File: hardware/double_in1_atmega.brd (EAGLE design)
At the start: 75 x 35 mm, 37 parts, among them IC1 MEGA8-AI, J1 AVR-ISP-6PINAVR-ISP-6PIN-SMAL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

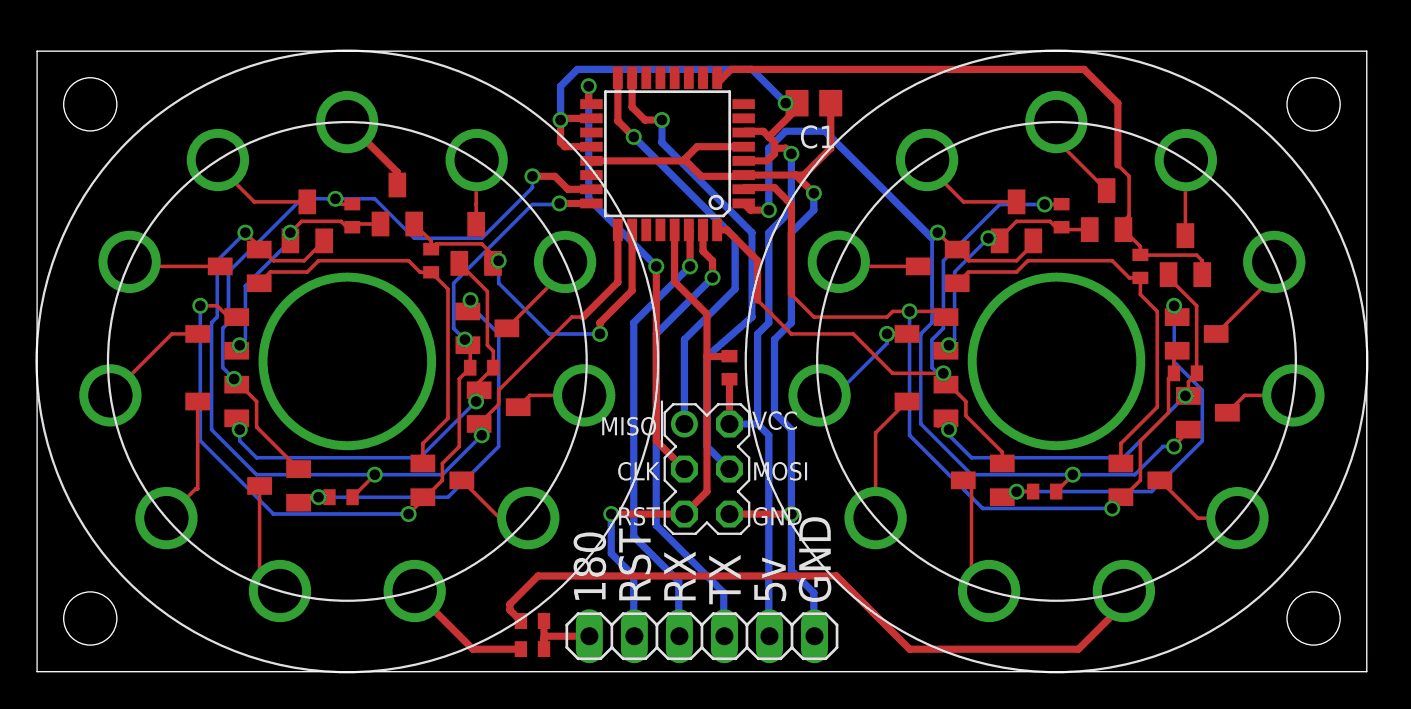
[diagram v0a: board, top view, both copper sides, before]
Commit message: [PCB] rev1; Change resistors size, center ATMEGA8, make slots for nixie alignment, minor changes
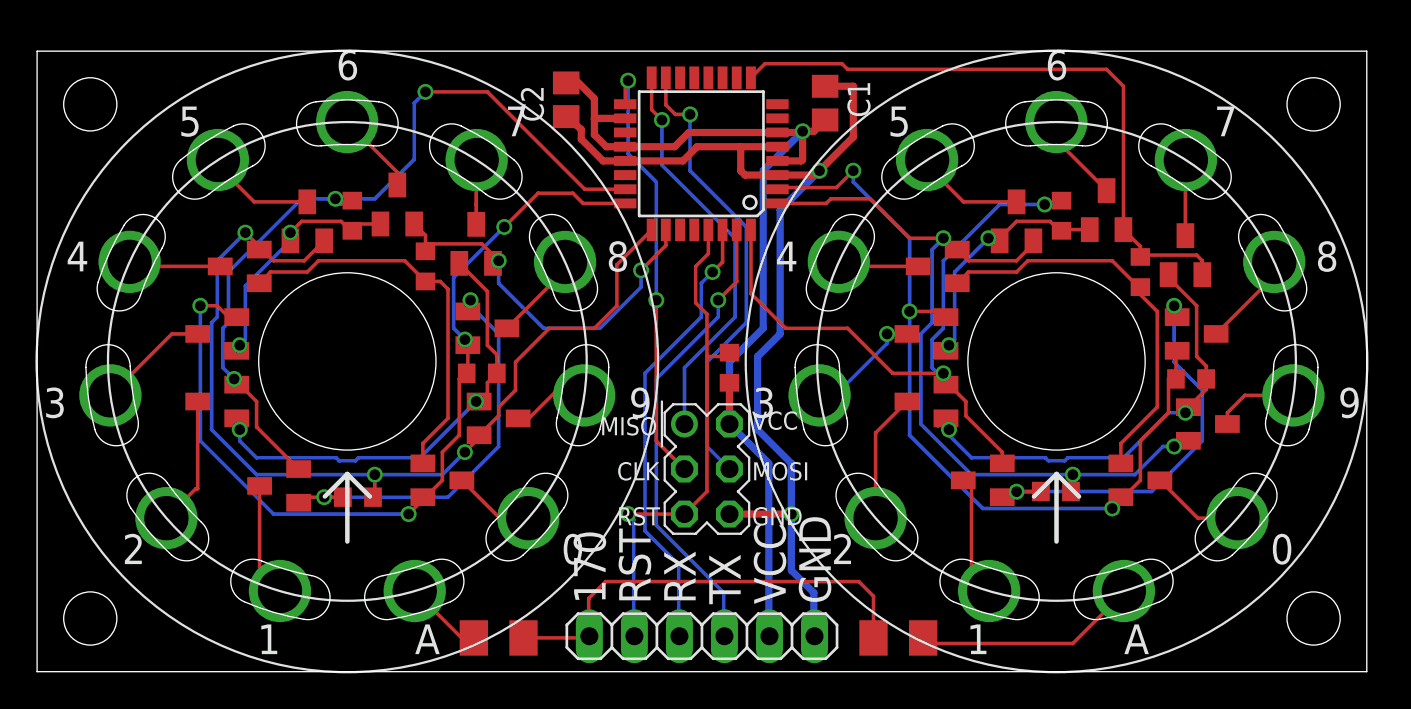
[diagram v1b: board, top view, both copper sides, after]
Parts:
- added C2: (no value), eagle-ltspice:C0805
- R1, R11, R2, R3, R4, R6, R7, R8, R9: device resistor:R0402 -> resistor:R0603
- R10, R5: device resistor:R0402 -> rcl:M1206
- U$1, U$2: device LC-516:LC-516 -> LC-516_play:LC-516
- moved R10 20.7 mm to (48.6, 1.91), turned to 180 degrees
- moved R5 2.01 mm to (26.0, 1.91)
- moved IC1 1.91 mm to (37.5, 29.2)
- moved R4 0.95 mm to (18.1, 9.84)
- moved C1 0.64 mm to (44.5, 32.1), turned to 270 degrees
- moved T13 0.63 mm to (66.0, 14.0)
- moved T4 0.63 mm to (26.0, 14.3)
- moved R9 0.63 mm to (57.5, 10.2)
- moved R6 0.45 mm to (65.1, 16.5)
- moved R3 0.45 mm to (21.9, 22.9)
- moved R1 0.32 mm to (25.1, 16.8)
- moved R8 0.32 mm to (62.2, 22.5)
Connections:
- net GND: now also C2.1
- net VCC: now also C2.2
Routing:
- net N$1: track 40.0 -> 12.7 mm
- net +15V: track 4.84 -> 25.1 mm
- net TSB4: track 53.7 -> 45.6 mm, vias 4 -> 3
- net GND: track 52.4 -> 59.4 mm
- net VCC: track 62.0 -> 56.3 mm, vias 3 -> 1
- net TSA2: track 39.7 -> 45.2 mm
- net TSA1: track 48.2 -> 51.6 mm
- net N$4: track 7.35 -> 4.43 mm
- net TSB3: track 38.0 -> 36.4 mm
- net N$2: track 30.1 -> 28.7 mm
- net TSA4: track 51.8 -> 53.3 mm
- net N$10: track 27.2 -> 25.9 mm
- net TSB1: track 39.7 -> 38.7 mm
- net N$5: track 23.5 -> 22.7 mm
- net N$17: track 13.6 -> 14.3 mm
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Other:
- board text added: "170"
- board text removed: "180"
- board text removed: "5v"
- board text removed: "Flayols - Bailly 12/17"

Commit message: generate gerber for jlpcb
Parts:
- added GOLD_ORB_SM1: OSHWLOGOLOGO5MM, oshw:OSHW_5MM
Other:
- board text added: "hackaday.io/project/69708 T Flayols - 2018"
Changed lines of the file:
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@@
 <?xml version="1.0" encoding="utf-8"?>
 <!DOCTYPE eagle SYSTEM "eagle.dtd">
-<eagle version="8.7.0">
+<eagle version="9.1.0">
 <drawing>
 <settings>
@@
 <layer number="48" name="Document" color="7" fill="1" visible="no" active="yes"/>
 <layer number="49" name="Reference" color="7" fill="1" visible="no" active="yes"/>
+<layer number="50" name="dxf" color="7" fill="1" visible="no" active="no"/>
 <layer number="51" name="tDocu" color="7" fill="1" visible="no" active="yes"/>
 <layer number="52" name="bDocu" color="7" fill="1" visible="no" active="yes"/>
+<layer number="53" name="tGND_GNDA" color="7" fill="9" visible="no" active="no"/>
+<layer number="54" name="bGND_GNDA" color="1" fill="9" visible="no" active="no"/>
+<layer number="56" name="wert" color="7" fill="1" visible="no" active="no"/>
+<layer number="90" name="Modules" color="5" fill="1" visible="no" active="no"/>
 <layer number="91" name="Nets" color="2" fill="1" visible="no" active="no"/>
 <layer number="92" name="Busses" color="1" fill="1" visible="no" active="no"/>
@@
 <layer number="98" name="Guide" color="6" fill="1" visible="no" active="no"/>
 <layer number="99" name="SpiceOrder" color="5" fill="1" visible="no" active="no"/>
+<layer number="100" name="Muster" color="7" fill="1" visible="no" active="no"/>
+<layer number="101" name="Patch_Top" color="12" fill="4" visible="yes" active="yes"/>
+<layer number="102" name="Vscore" color="7" fill="1" visible="yes" active="yes"/>
+<layer number="103" name="tMap" color="7" fill="1" visible="yes" active="yes"/>
+<layer number="104" name="Name" color="7" fill="1" visible="yes" active="yes"/>
+<layer number="105" name="tPlate" color="7" fill="1" visible="yes" active="yes"/>
+<layer number="106" name="bPlate" color="7" fill="1" visible="yes" active="yes"/>
+<layer number="107" name="Crop" color="7" fill="1" visible="yes" active="yes"/>
+<layer number="116" name="Patch_BOT" color="9" fill="4" visible="yes" active="yes"/>
+<layer number="121" name="_tsilk" color="7" fill="1" visible="yes" active="yes"/>
+<layer number="122" name="_bsilk" color="7" fill="1" visible="yes" active="yes"/>
+<layer number="125" name="_tNames" color="7" fill="1" visible="yes" active="yes"/>
+<layer number="144" name="Drill_legend" color="7" fill="1" visible="yes" active="yes"/>
+<layer number="151" name="HeatSink" color="7" fill="1" visible="yes" active="yes"/>
+<layer number="200" name="200bmp" color="1" fill="10" visible="yes" active="yes"/>
+<layer number="201" name="201bmp" color="2" fill="1" visible="no" active="no"/>
+<layer number="202" name="202bmp" color="3" fill="1" visible="no" active="no"/>
+<layer number="203" name="203bmp" color="4" fill="10" visible="yes" active="yes"/>
+<layer number="204" name="204bmp" color="5" fill="10" visible="yes" active="yes"/>
+<layer number="205" name="205bmp" color="6" fill="10" visible="yes" active="yes"/>
+<layer number="206" name="206bmp" color="7" fill="10" visible="yes" active="yes"/>
+<layer number="207" name="207bmp" color="8" fill="10" visible="yes" active="yes"/>
+<layer number="208" name="208bmp" color="9" fill="10" visible="yes" active="yes"/>
+<layer number="209" name="209bmp" color="7" fill="1" visible="yes" active="yes"/>
+<layer number="210" name="210bmp" color="7" fill="1" visible="yes" active="yes"/>
+<layer number="211" name="211bmp" color="7" fill="1" visible="yes" active="yes"/>
+<layer number="212" name="212bmp" color="7" fill="1" visible="yes" active="yes"/>
+<layer number="213" name="213bmp" color="7" fill="1" visible="yes" active="yes"/>
+<layer number="214" name="214bmp" color="7" fill="1" visible="yes" active="yes"/>
+<layer number="215" name="215bmp" color="7" fill="1" visible="yes" active="yes"/>
+<layer number="216" name="216bmp" color="7" fill="1" visible="yes" active="yes"/>
+<layer number="250" name="Descript" color="3" fill="1" visible="no" active="no"/>
+<layer number="251" name="SMDround" color="12" fill="11" visible="no" active="no"/>
+<layer number="254" name="cooling" color="7" fill="1" visible="yes" active="yes"/>
 </layers>
 <board>
@@
 <text x="40.3225" y="8.255" size="1.016" layer="25" font="vector">GND</text>
 <text x="40.3225" y="10.795" size="1.016" layer="25" font="vector">MOSI</text>
+<text x="37.338" y="33.147" size="1.016" layer="26" font="vector" rot="MR180" align="center">hackaday.io/project/69708
+T Flayols - 2018</text>
 </plain>
 <attributes>
@@
 <param name="checkStop" value="0"/>
 <param name="checkValues" value="0"/>
+<param name="checkNames" value="1"/>
+<param name="checkWireStubs" value="1"/>
+<param name="checkPolygonWidth" value="0"/>
 <param name="useDiameter" value="13"/>
 <param name="maxErrors" value="50"/>
@@
 <attribute name="VALUE" x="37.0205" y="17.78" size="1.27" layer="27" rot="R270"/>
 </element>
-<element name="C1" library="eagle-ltspice" library_urn="urn:adsk.eagle:library:217" package="C0805" package3d_urn="urn:adsk.eagle:package:13265/1" value="" x="44.45" y="32.0675" rot="R270">
+<element name="C1" library="eagle-ltspice" library_urn="urn:adsk.eagle:library:217" package="C0805" package3d_urn="urn:adsk.eagle:package:13265/1" value="" x="44.45" y="32.0675" smashed="yes" rot="R270">
 <attribute name="SPICEMODEL" value="NONE" x="44.45" y="32.0675" size="1.778" layer="27" rot="R270" display="off"/>
 <attribute name="SPICEPREFIX" value="C" x="44.45" y="32.0675" size="1.778" layer="27" rot="R270" display="off"/>
+<attribute name="VALUE" x="41.91" y="33.3375" size="1.27" layer="27" rot="R270"/>
 </element>
 <element name="U$1" library="LC-516_play" package="LC-516" value="LC-516" x="17.5" y="17.5" locked="yes"/>
 <element name="U$2" library="LC-516_play" package="LC-516" value="LC-516" x="57.5" y="17.5" locked="yes"/>
-<element name="C2" library="eagle-ltspice" library_urn="urn:adsk.eagle:library:217" package="C0805" package3d_urn="urn:adsk.eagle:package:13265/1" value="" x="29.845" y="32.258" rot="R90">
+<element name="C2" library="eagle-ltspice" library_urn="urn:adsk.eagle:library:217" package="C0805" package3d_urn="urn:adsk.eagle:package:13265/1" value="" x="29.845" y="32.258" smashed="yes" rot="R90">
 <attribute name="SPICEMODEL" value="NONE" x="29.845" y="32.258" size="1.778" layer="27" rot="R90" display="off"/>
 <attribute name="SPICEPREFIX" value="C" x="29.845" y="32.258" size="1.778" layer="27" rot="R90" display="off"/>
-</element>
+<attribute name="VALUE" x="32.385" y="30.988" size="1.27" layer="27" rot="R90"/>
+</element>
+<element name="GOLD_ORB_SM1" library="oshw" package="OSHW_5MM" value="OSHWLOGOLOGO5MM" x="37.465" y="29.083" smashed="yes" rot="MR0"/>
 </elements>
 <signals>
@@
 <wire x1="50.8" y1="20.32" x2="49.2125" y2="20.32" width="0.2032" layer="1"/>
 <via x="46.0375" y="28.2575" extent="1-16" drill="0.6"/>
-<wire x1="42.81599375" y1="27.305" x2="42.88739375" y2="27.2336" width="0.2032" layer="1"/>
 <wire x1="41.5925" y1="27.305" x2="42.81599375" y2="27.305" width="0.2032" layer="1"/>
 <wire x1="49.2125" y1="20.32" x2="49.2125" y2="24.4475" width="0.2032" layer="16"/>
@@
 </signal>
 </signals>
+<mfgpreviewcolors>
+<mfgpreviewcolor name="soldermaskcolor" color="0xC8008000"/>
+<mfgpreviewcolor name="silkscreencolor" color="0xFFFEFEFE"/>
+<mfgpreviewcolor name="backgroundcolor" color="0xFF282828"/>
+<mfgpreviewcolor name="coppercolor" color="0xFFFFBF00"/>
+<mfgpreviewcolor name="substratecolor" color="0xFF786E46"/>
+</mfgpreviewcolors>
 </board>
 </drawing>
 <compatibility>
+<note version="6.3" minversion="6.2.2" severity="warning">
+Since Version 6.2.2 text objects can contain more than one line,
+which will not be processed correctly with this version.
+</note>
 <note version="8.2" severity="warning">
 Since Version 8.2, EAGLE supports online libraries. The ids
